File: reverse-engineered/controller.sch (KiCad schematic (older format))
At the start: 12 parts

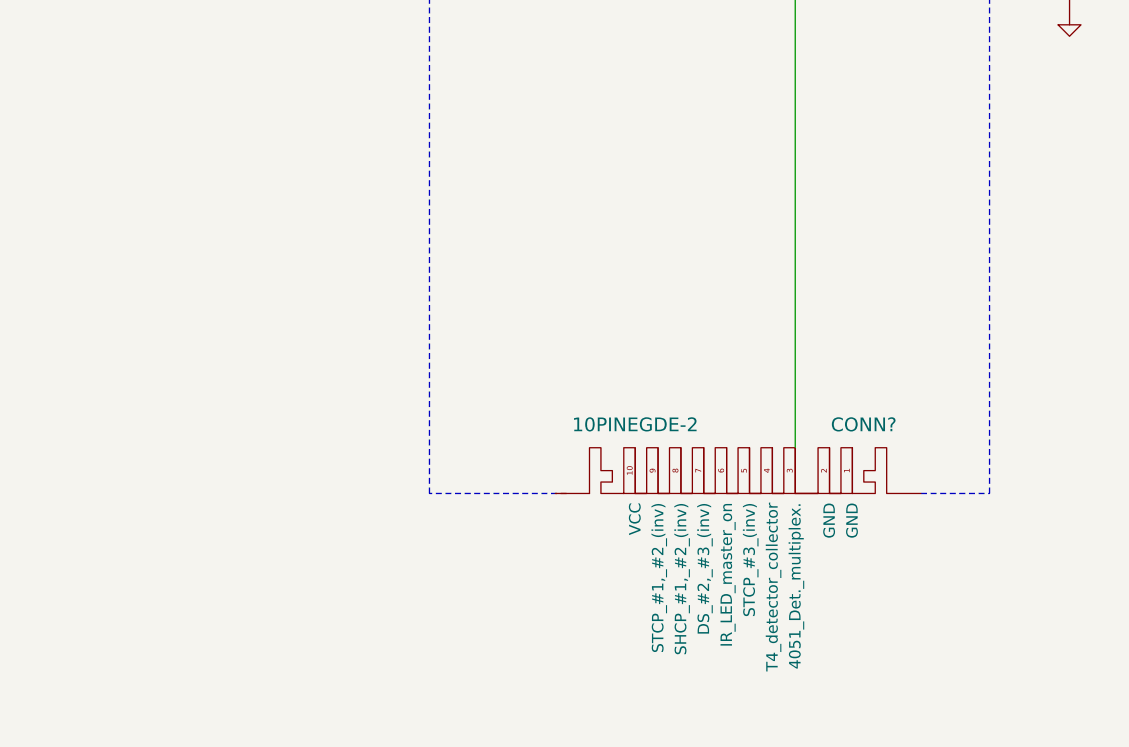
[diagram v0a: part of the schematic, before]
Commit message: Some more reverse engineering
Started measure with oscilloscope, seems
to get funny measurements. Will have to do
them again.
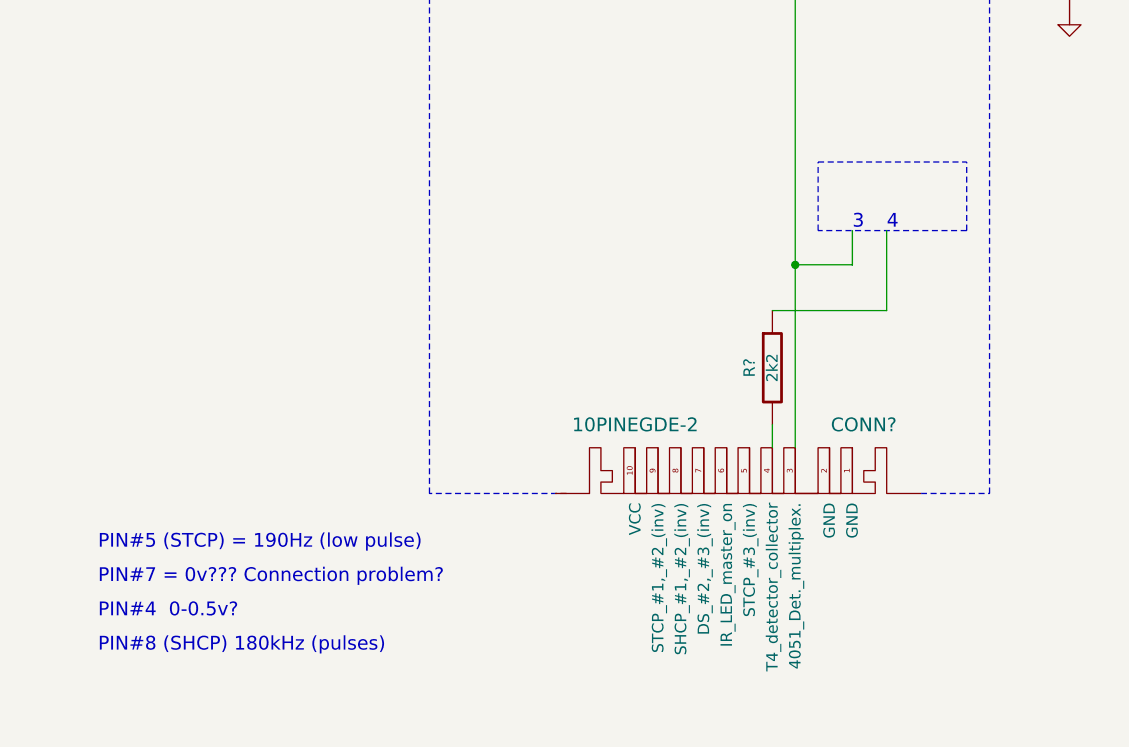
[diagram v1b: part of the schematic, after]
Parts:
- added R?: 2k2, symbol R
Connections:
- wire segments 24 -> 29
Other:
- note added: "3"
- note added: "4"
- note added: "PIN#4 0-0.5v?"
- note added: "PIN#5 (STCP) = 190Hz (low pulse)"
- note added: "PIN#7 = 0v??? Connection problem?"
- note added: "PIN#8 (SHCP) 180kHz (pulses)"
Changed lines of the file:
@@
-EESchema Schematic File Version 2  date Thu 13 Dec 2012 01:05:19 PM CET
+EESchema Schematic File Version 2  date Mon 29 Apr 2013 10:24:02 PM CEST
 LIBS:power
 LIBS:device
@@
 LIBS:contrib
 LIBS:valves
-LIBS:kicad-components
 LIBS:reversed-engineered-cache
 EELAYER 25  0
@@
 Sheet 4 6
 Title ""
-Date "13 dec 2012"
+Date "29 apr 2013"
 Rev ""
 Comp ""
@@
 Comment4 ""
 $EndDescr
-Text Label 4900 3300 0    60   ~ 0
-AION0
+Text Notes 2600 7500 0    60   ~ 0
+PIN#8 (SHCP) 180kHz (pulses)
+Text Notes 2600 7350 0    60   ~ 0
+PIN#4  0-0.5v?
+Text Notes 2600 7200 0    60   ~ 0
+PIN#7 = 0v??? Connection problem?
+Text Notes 2600 7050 0    60   ~ 0
+PIN#5 (STCP) = 190Hz (low pulse)
+Text Notes 6050 5650 0    60   ~ 0
+4
+Wire Wire Line
+	6050 5650 6050 6000
+Wire Wire Line
+	6050 6000 5550 6000
+Connection ~ 5650 5800
+Wire Wire Line
+	5650 5800 5900 5800
+Wire Wire Line
+	5900 5800 5900 5650
 Wire Wire Line
 	4950 2350 4800 2350
@@
 Wire Wire Line
 	6850 3850 6850 3950
+Wire Notes Line
+	6400 5650 6400 5350
+Wire Notes Line
+	6400 5650 5750 5650
+Wire Notes Line
+	5750 5650 5750 5350
+Wire Notes Line
+	5750 5350 6400 5350
+Wire Wire Line
+	5550 6500 5550 6600
 $Comp
 L R R?
+U 1 1 517EC305
+P 5550 6250
+F 0 "R?" V 5450 6250 50  0000 C CNN
+F 1 "2k2" V 5550 6250 50  0000 C CNN
+	1    5550 6250
+	1    0    0    -1
+$EndComp
+Text Notes 5900 5650 0    60   ~ 0
+3
+Text Label 4900 3300 0    60   ~ 0
+AION0
+$Comp
+L R R?
